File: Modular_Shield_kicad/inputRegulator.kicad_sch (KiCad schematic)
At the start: 4 parts

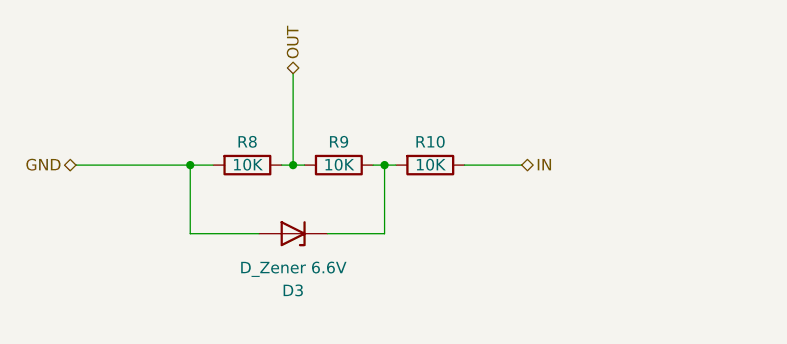
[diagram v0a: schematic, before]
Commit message: [UDPT] Kicad Project name
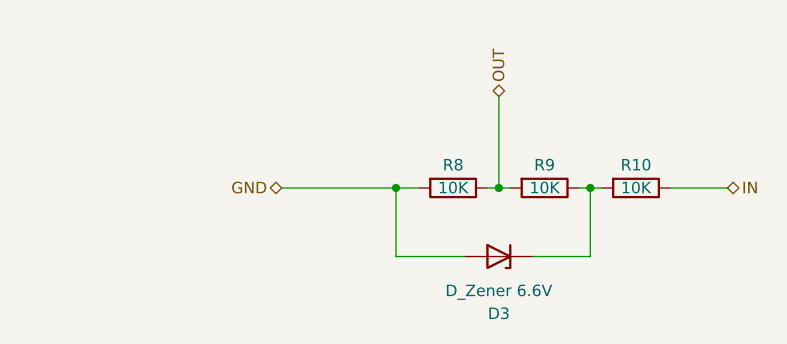
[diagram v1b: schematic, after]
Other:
- moved on the sheet: D3, R10, R8, R9
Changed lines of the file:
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@@
 (kicad_sch (version 20230121) (generator eeschema)
-  (paper "A4")
-  (junction (at 33.02 30.48) (diameter 0) (color 0 0 0 0)
-  )
-  (junction (at 54.61 30.48) (diameter 0) (color 0 0 0 0)
-  )
-  (junction (at 44.45 30.48) (diameter 0) (color 0 0 0 0)
-  )
-  (wire (pts (xy 43.18 30.48) (xy 44.45 30.48))
-    (stroke (width 0) (type default))
-  )
-  (wire (pts (xy 33.02 30.48) (xy 35.56 30.48))
-    (stroke (width 0) (type default))
-  )
-  (wire (pts (xy 54.61 38.1) (xy 54.61 30.48))
-    (stroke (width 0) (type default))
-  )
-  (wire (pts (xy 54.61 30.48) (xy 53.34 30.48))
-    (stroke (width 0) (type default))
-  )
-  (wire (pts (xy 33.02 38.1) (xy 33.02 30.48))
-    (stroke (width 0) (type default))
-  )
-  (wire (pts (xy 44.45 30.48) (xy 45.72 30.48))
-    (stroke (width 0) (type default))
-  )
-  (wire (pts (xy 55.88 30.48) (xy 54.61 30.48))
-    (stroke (width 0) (type default))
-  )
-  (wire (pts (xy 20.32 30.48) (xy 33.02 30.48))
-    (stroke (width 0) (type default))
-  )
-  (wire (pts (xy 40.64 38.1) (xy 33.02 38.1))
-    (stroke (width 0) (type default))
-  )
-  (wire (pts (xy 44.45 20.32) (xy 44.45 30.48))
-    (stroke (width 0) (type default))
-  )
-  (wire (pts (xy 48.26 38.1) (xy 54.61 38.1))
-    (stroke (width 0) (type default))
-  )
-  (wire (pts (xy 63.5 30.48) (xy 69.85 30.48))
-    (stroke (width 0) (type default))
-  )
-  (hierarchical_label "OUT" (shape bidirectional) (at 44.45 20.32 90) (fields_autoplaced)
+  (paper "User" 132.004 99.9998)
+  (junction (at 55.88 33.02) (diameter 0) (color 0 0 0 0)
+  )
+  (junction (at 77.47 33.02) (diameter 0) (color 0 0 0 0)
+  )
+  (junction (at 67.31 33.02) (diameter 0) (color 0 0 0 0)
+  )
+  (wire (pts (xy 66.04 33.02) (xy 67.31 33.02))
+    (stroke (width 0) (type default))
+  )
+  (wire (pts (xy 55.88 33.02) (xy 58.42 33.02))
+    (stroke (width 0) (type default))
+  )
+  (wire (pts (xy 77.47 40.64) (xy 77.47 33.02))
+    (stroke (width 0) (type default))
+  )
+  (wire (pts (xy 77.47 33.02) (xy 76.2 33.02))
+    (stroke (width 0) (type default))
+  )
+  (wire (pts (xy 55.88 40.64) (xy 55.88 33.02))
+    (stroke (width 0) (type default))
+  )
+  (wire (pts (xy 67.31 33.02) (xy 68.58 33.02))
+    (stroke (width 0) (type default))
+  )
+  (wire (pts (xy 78.74 33.02) (xy 77.47 33.02))
+    (stroke (width 0) (type default))
+  )
+  (wire (pts (xy 43.18 33.02) (xy 55.88 33.02))
+    (stroke (width 0) (type default))
+  )
+  (wire (pts (xy 63.5 40.64) (xy 55.88 40.64))
+    (stroke (width 0) (type default))
+  )
+  (wire (pts (xy 67.31 22.86) (xy 67.31 33.02))
+    (stroke (width 0) (type default))
+  )
+  (wire (pts (xy 71.12 40.64) (xy 77.47 40.64))
+    (stroke (width 0) (type default))
+  )
+  (wire (pts (xy 86.36 33.02) (xy 92.71 33.02))
+    (stroke (width 0) (type default))
+  )
+  (hierarchical_label "OUT" (shape bidirectional) (at 67.31 22.86 90) (fields_autoplaced)
     (effects (font (size 1.27 1.27)) (justify left))
   )
-  (hierarchical_label "IN" (shape bidirectional) (at 69.85 30.48 0) (fields_autoplaced)
+  (hierarchical_label "IN" (shape bidirectional) (at 92.71 33.02 0) (fields_autoplaced)
     (effects (font (size 1.27 1.27)) (justify left))
   )
-  (hierarchical_label "GND" (shape bidirectional) (at 20.32 30.48 180) (fields_autoplaced)
+  (hierarchical_label "GND" (shape bidirectional) (at 43.18 33.02 180) (fields_autoplaced)
     (effects (font (size 1.27 1.27)) (justify right))
   )
-  (symbol (lib_id "Modular Shield:R") (at 49.53 30.48 270) (unit 1)
-    (in_bom yes) (on_board yes) (dnp no)
-    (property "Reference" "R9" (at 49.53 27.94 90)
-      (effects (font (size 1.27 1.27)))
-    )
-    (property "Value" "10K" (at 49.53 30.48 90)
-      (effects (font (size 1.27 1.27)))
-    )
-    (property "Footprint" "Modular Shield:R_0603_1608Metric" (at 49.53 28.702 90)
-      (effects (font (size 1.27 1.27)) hide)
-    )
-    (property "Datasheet" "~" (at 49.53 30.48 0)
-      (effects (font (size 1.27 1.27)) hide)
-    )
-    (property "LCSC" "C25804" (at 49.53 34.29 90)
-      (effects (font (size 1.27 1.27)) hide)
-    )
-    (pin "1")
-    (pin "2")
-    (instances
-      (project "Raspberry_modular"
+  (symbol (lib_id "Modular Shield:R") (at 72.39 33.02 270) (unit 1)
+    (in_bom yes) (on_board yes) (dnp no)
+    (property "Reference" "R9" (at 72.39 30.48 90)
+      (effects (font (size 1.27 1.27)))
+    )
+    (property "Value" "10K" (at 72.39 33.02 90)
+      (effects (font (size 1.27 1.27)))
+    )
+    (property "Footprint" "Modular Shield:R_0603_1608Metric" (at 72.39 31.242 90)
+      (effects (font (size 1.27 1.27)) hide)
+    )
+    (property "Datasheet" "~" (at 72.39 33.02 0)
+      (effects (font (size 1.27 1.27)) hide)
+    )
+    (property "LCSC" "C25804" (at 72.39 36.83 90)
+      (effects (font (size 1.27 1.27)) hide)
+    )
+    (pin "1")
+    (pin "2")
+    (instances
+      (project "Modular_Shield"
         (path "/f7f606ea-7d0c-4680-9293-4d1bbfd60125/00000000-0000-0000-0000-00006224fa7b"
           (reference "R9") (unit 1)
@@
     )
   )
-  (symbol (lib_id "Modular Shield:R") (at 59.69 30.48 270) (unit 1)
-    (in_bom yes) (on_board yes) (dnp no)
-    (property "Reference" "R10" (at 59.69 27.94 90)
-      (effects (font (size 1.27 1.27)))
-    )
-    (property "Value" "10K" (at 59.69 30.48 90)
-      (effects (font (size 1.27 1.27)))
-    )
-    (property "Footprint" "Modular Shield:R_0603_1608Metric" (at 59.69 28.702 90)
-      (effects (font (size 1.27 1.27)) hide)
-    )
-    (property "Datasheet" "~" (at 59.69 30.48 0)
-      (effects (font (size 1.27 1.27)) hide)
-    )
-    (property "LCSC" "C25804" (at 59.69 34.29 90)
-      (effects (font (size 1.27 1.27)) hide)
-    )
-    (pin "1")
-    (pin "2")
-    (instances
-      (project "Raspberry_modular"
+  (symbol (lib_id "Modular Shield:R") (at 82.55 33.02 270) (unit 1)
+    (in_bom yes) (on_board yes) (dnp no)
+    (property "Reference" "R10" (at 82.55 30.48 90)
+      (effects (font (size 1.27 1.27)))
+    )
+    (property "Value" "10K" (at 82.55 33.02 90)
+      (effects (font (size 1.27 1.27)))
+    )
+    (property "Footprint" "Modular Shield:R_0603_1608Metric" (at 82.55 31.242 90)
+      (effects (font (size 1.27 1.27)) hide)
+    )
+    (property "Datasheet" "~" (at 82.55 33.02 0)
+      (effects (font (size 1.27 1.27)) hide)
+    )
+    (property "LCSC" "C25804" (at 82.55 36.83 90)
+      (effects (font (size 1.27 1.27)) hide)
+    )
+    (pin "1")
+    (pin "2")
+    (instances
+      (project "Modular_Shield"
         (path "/f7f606ea-7d0c-4680-9293-4d1bbfd60125/00000000-0000-0000-0000-00006224fa7b"
           (reference "R10") (unit 1)
@@
     )
   )
-  (symbol (lib_id "Modular Shield:R") (at 39.37 30.48 270) (unit 1)
-    (in_bom yes) (on_board yes) (dnp no)
-    (property "Reference" "R8" (at 39.37 27.94 90)
-      (effects (font (size 1.27 1.27)))
-    )
-    (property "Value" "10K" (at 39.37 30.48 90)
-      (effects (font (size 1.27 1.27)))
-    )
-    (property "Footprint" "Modular Shield:R_0603_1608Metric" (at 39.37 28.702 90)
-      (effects (font (size 1.27 1.27)) hide)
-    )
-    (property "Datasheet" "~" (at 39.37 30.48 0)
-      (effects (font (size 1.27 1.27)) hide)
-    )
-    (property "LCSC" "C25804" (at 39.37 34.29 90)
-      (effects (font (size 1.27 1.27)) hide)
-    )
-    (pin "1")
-    (pin "2")
-    (instances
-      (project "Raspberry_modular"
+  (symbol (lib_id "Modular Shield:R") (at 62.23 33.02 270) (unit 1)
+    (in_bom yes) (on_board yes) (dnp no)
+    (property "Reference" "R8" (at 62.23 30.48 90)
+      (effects (font (size 1.27 1.27)))
+    )
+    (property "Value" "10K" (at 62.23 33.02 90)
+      (effects (font (size 1.27 1.27)))
+    )
+    (property "Footprint" "Modular Shield:R_0603_1608Metric" (at 62.23 31.242 90)
+      (effects (font (size 1.27 1.27)) hide)
+    )
+    (property "Datasheet" "~" (at 62.23 33.02 0)
+      (effects (font (size 1.27 1.27)) hide)
+    )
+    (property "LCSC" "C25804" (at 62.23 36.83 90)
+      (effects (font (size 1.27 1.27)) hide)
+    )
+    (pin "1")
+    (pin "2")
+    (instances
+      (project "Modular_Shield"
         (path "/f7f606ea-7d0c-4680-9293-4d1bbfd60125/00000000-0000-0000-0000-00006224fa7b"
           (reference "R8") (unit 1)
@@
     )
   )
-  (symbol (lib_id "Modular Shield:D_Zener") (at 44.45 38.1 180) (unit 1)
-    (in_bom yes) (on_board yes) (dnp no)
-    (property "Reference" "D3" (at 44.45 44.45 0)
-      (effects (font (size 1.27 1.27)))
-    )
-    (property "Value" "D_Zener 6.6V" (at 44.45 41.91 0)
-      (effects (font (size 1.27 1.27)))
-    )
-    (property "Footprint" "Modular Shield:D_0603_1608Metric" (at 44.45 38.1 0)
-      (effects (font (size 1.27 1.27)) hide)
-    )
-    (property "Datasheet" "~" (at 44.45 38.1 0)
-      (effects (font (size 1.27 1.27)) hide)
-    )
-    (property "LCSC" "C894569" (at 44.45 44.45 0)
-      (effects (font (size 1.27 1.27)) hide)
-    )
-    (pin "1")
-    (pin "2")
-    (instances
-      (project "Raspberry_modular"
+  (symbol (lib_id "Modular Shield:D_Zener") (at 67.31 40.64 180) (unit 1)
+    (in_bom yes) (on_board yes) (dnp no)
+    (property "Reference" "D3" (at 67.31 46.99 0)
+      (effects (font (size 1.27 1.27)))
+    )
+    (property "Value" "D_Zener 6.6V" (at 67.31 44.45 0)
+      (effects (font (size 1.27 1.27)))
+    )
+    (property "Footprint" "Modular Shield:D_0603_1608Metric" (at 67.31 40.64 0)
+      (effects (font (size 1.27 1.27)) hide)
+    )
+    (property "Datasheet" "~" (at 67.31 40.64 0)
+      (effects (font (size 1.27 1.27)) hide)
+    )
+    (property "LCSC" "C894569" (at 67.31 46.99 0)
+      (effects (font (size 1.27 1.27)) hide)
+    )
+    (pin "1")
+    (pin "2")
+    (instances
+      (project "Modular_Shield"
         (path "/f7f606ea-7d0c-4680-9293-4d1bbfd60125/00000000-0000-0000-0000-00006224fa7b"
           (reference "D3") (unit 1)
